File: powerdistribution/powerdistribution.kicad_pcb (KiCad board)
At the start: 4 copper layers, 110 x 75 mm, 128 parts, among them IC1 NCP718ASNADJT1G, J1 282837-2, J2 282837-2, J3 ESQ-113-12-G-D, J6 Conn_01x02, M1 Motor_Servo, M2 Motor_Servo, Q1 IRLML0030, Q2 IRLML0030, Q3 IRLML0030, Q5 IRLML0030, U1 BQ7790512PW, U10 TPS1HC30BQPWPRQ1, U3 AP64501QSP-13, U4 AP64501QSP-13, U5 TPS1HC30BQPWPRQ1, U6 TPS1HC30BQPWPRQ1, U9 MIC29302AWD-TR

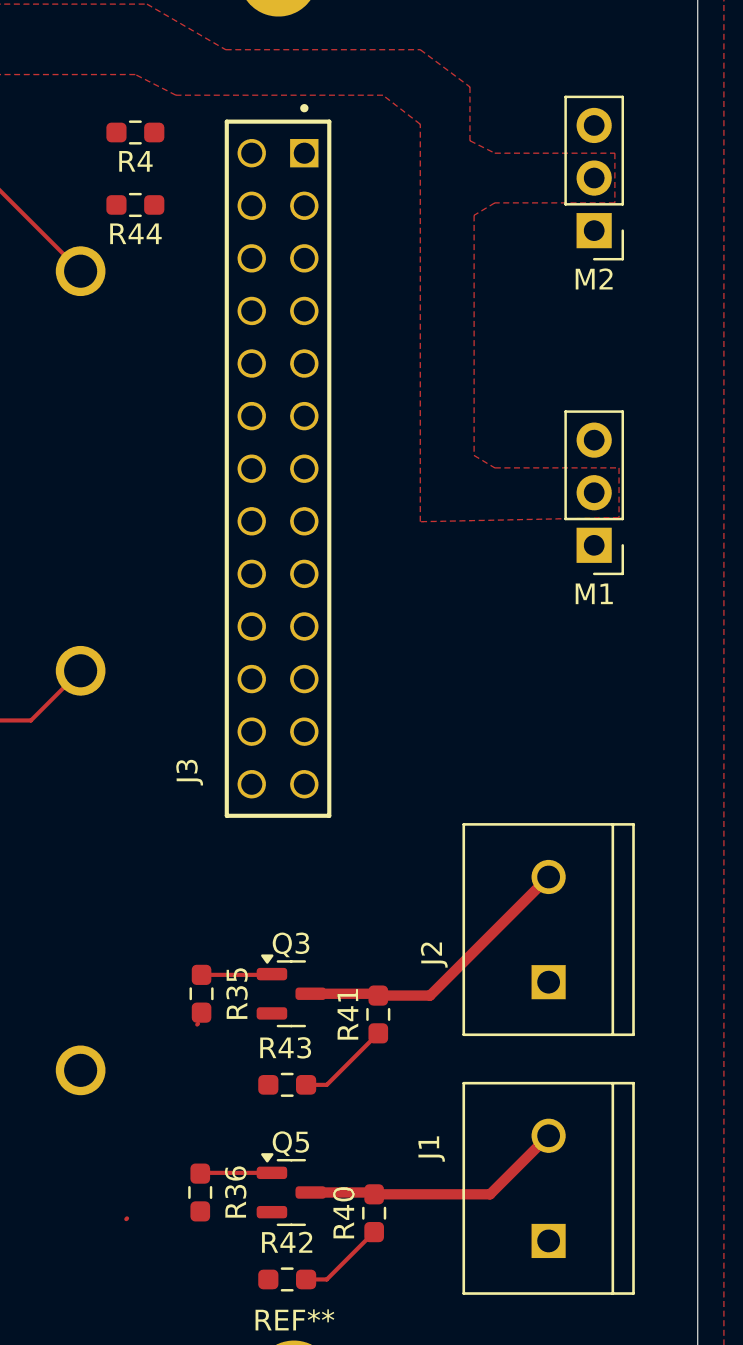
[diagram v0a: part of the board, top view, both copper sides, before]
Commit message: clean up, aligning connectors and board coordinates between fc and power board
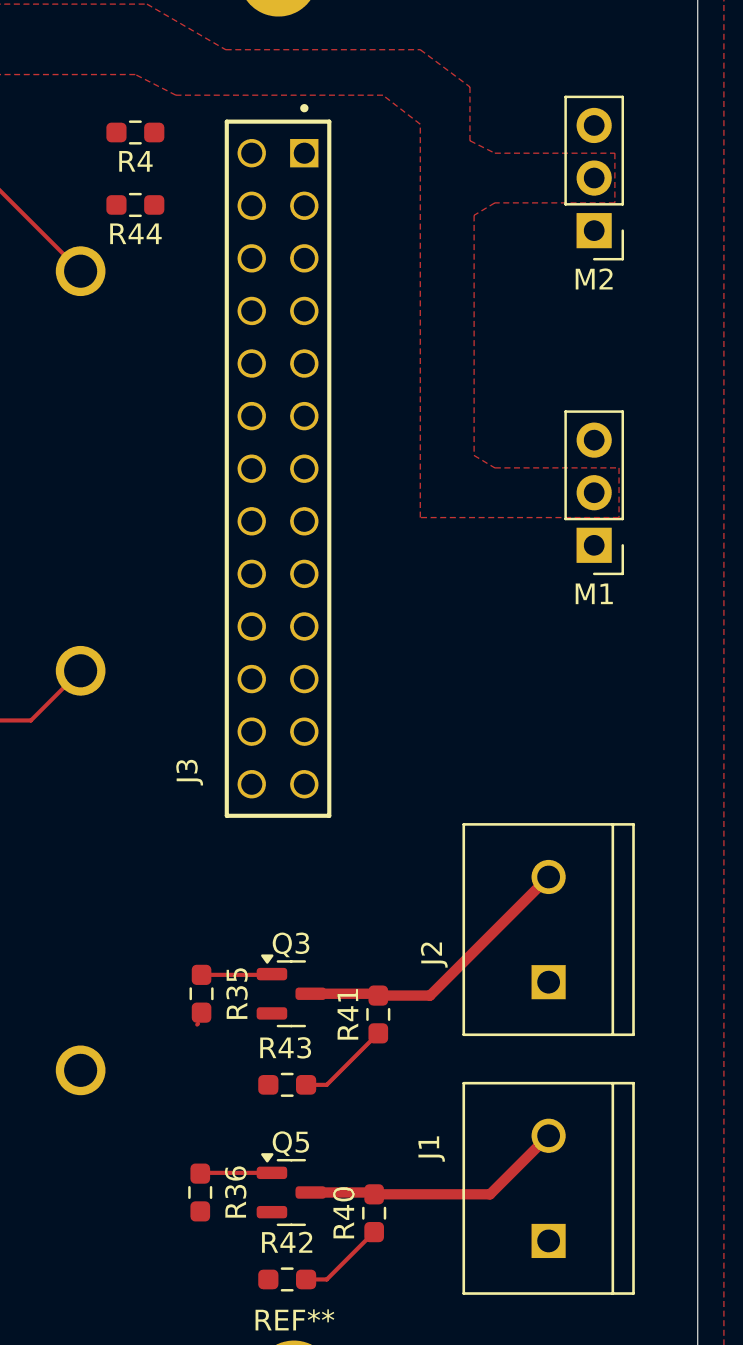
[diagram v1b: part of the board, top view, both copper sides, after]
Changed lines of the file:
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@@
-	)
-	(segment
-		(start 117.4375 126.45)
-		(end 117.4 126.4875)
-		(width 0.2)
-		(layer "F.Cu")
-		(net 21)
 	)
 	(segment
@@
 				(xy 71 69.8) (xy 74 69.8) (xy 75.8 67.8) (xy 118.4 67.8) (xy 122.2 70) (xy 131.6 70) (xy 134 71.8)
 				(xy 134 74.4) (xy 135.2 75) (xy 141 75) (xy 141 77.4) (xy 135.2 77.4) (xy 134.2 78) (xy 134.2 89.6)
-				(xy 135.2 90.2) (xy 141.2 90.2) (xy 141.2 92.6) (xy 131.6 92.8) (xy 131.6 73.6) (xy 129.8 72.2)
+				(xy 135.2 90.2) (xy 141.2 90.2) (xy 141.2 92.6) (xy 131.6 92.6) (xy 131.6 73.6) (xy 129.8 72.2)
 				(xy 119.8 72.2) (xy 117.8375 71.2) (xy 71 71.2)
 			)

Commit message: pd placement finish
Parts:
- removed R4, R44: 0, Resistor_SMD:R_0603_1608Metric_Pad0.98x0.95mm_HandSolder
- added J4: XT60-M, HPRfootprints:AMASS_XT60-M, F.Cu at (139.2, 103.6)
- added TP9: TestPoint, TestPoint:TestPoint_Pad_D2.0mm, F.Cu at (102.0, 104.0)
- added U11: S2P-VH, HPRfootprints:S2P-VH_JST, F.Cu at (132.2, 91.1)
- moved J6 77.8 mm to (136.2, 66.0)
- moved M1 15.6 mm to (135.5, 79.0), turned to 90 degrees
- moved M2 6.59 mm to (135.4, 74.0), turned to 90 degrees
- moved J2 6.29 mm to (138.5, 118.8)
- moved J1 5.25 mm to (137.8, 130.2)
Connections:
- J3 pad 01: unconnected-(J3-Pad01) -> /teensy_3.3v
- J3 pad 02: unconnected-(J3-Pad02) -> /6v_fault
- J3 pad 03: unconnected-(J3-Pad03) -> /servo2_pwm
- J3 pad 04: unconnected-(J3-Pad04) -> /6v_cursns
- J3 pad 05: unconnected-(J3-Pad05) -> /servo1_pwm
- J3 pad 06: unconnected-(J3-Pad06) -> /12v_fault
- J3 pad 08: unconnected-(J3-Pad08) -> /12v_cursns
- J3 pad 10: unconnected-(J3-Pad10) -> /5v_fault
- J3 pad 11: unconnected-(J3-Pad11) -> /PYRO1
- J3 pad 12: unconnected-(J3-Pad12) -> /5v_cursns
- J3 pad 13: unconnected-(J3-Pad13) -> /PYRO1CONN
- J3 pad 14: unconnected-(J3-Pad14) -> /SENSE_mosi
- J3 pad 15: unconnected-(J3-Pad15) -> /PYRO2
- J3 pad 16: unconnected-(J3-Pad16) -> /SENSE_miso
- J3 pad 17: unconnected-(J3-Pad17) -> /PYRO2CONN
- J3 pad 18: unconnected-(J3-Pad18) -> /SENSE_sck
- J3 pad 19: unconnected-(J3-Pad19) -> /5V
- J3 pad 20: unconnected-(J3-Pad20) -> GND
- J3 pad 21: unconnected-(J3-Pad21) -> /5V
- J3 pad 22: unconnected-(J3-Pad22) -> GND
- J3 pad 23: unconnected-(J3-Pad23) -> /5V
- J3 pad 24: unconnected-(J3-Pad24) -> GND
- J3 pad 26: unconnected-(J3-Pad26) -> GND
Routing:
- net /LDO_5V: track 7.42 -> 92.9 mm, vias 1 -> 7
- net /5v_cursns: track 2.98 -> 85.2 mm, vias 0 -> 1
- net /5v_fault: track 0.00 -> 80.7 mm, vias 0 -> 1
- net /12v_cursns: track 2.48 -> 79.1 mm, vias 0 -> 1
- net /12v_fault: track 0.00 -> 74.6 mm, vias 0 -> 1
- net /6v_cursns: track 2.73 -> 73.4 mm, vias 0 -> 1
- net /6v_fault: track 0.00 -> 69.2 mm, vias 0 -> 1
- net /PYRO1CONN: track 4.24 -> 46.6 mm, vias 0 -> 1
- net /PYRO1: track 3.42 -> 41.2 mm, vias 0 -> 1
- net /PYRO2CONN: track 4.52 -> 28.2 mm, vias 0 -> 1
- net /PYRO2: track 3.36 -> 26.1 mm, vias 0 -> 1
- net /servo2_pwm: track 0.00 -> 10.9 mm
- net /servo1_pwm: track 0.00 -> 9.95 mm
- net /Pack+: track 23.9 -> 16.3 mm
- net /5V_DIAGEN: track 7.52 -> 12.7 mm
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- added copper zone on F.Cu, net /5V
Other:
- board text removed: "${REFERENCE}"

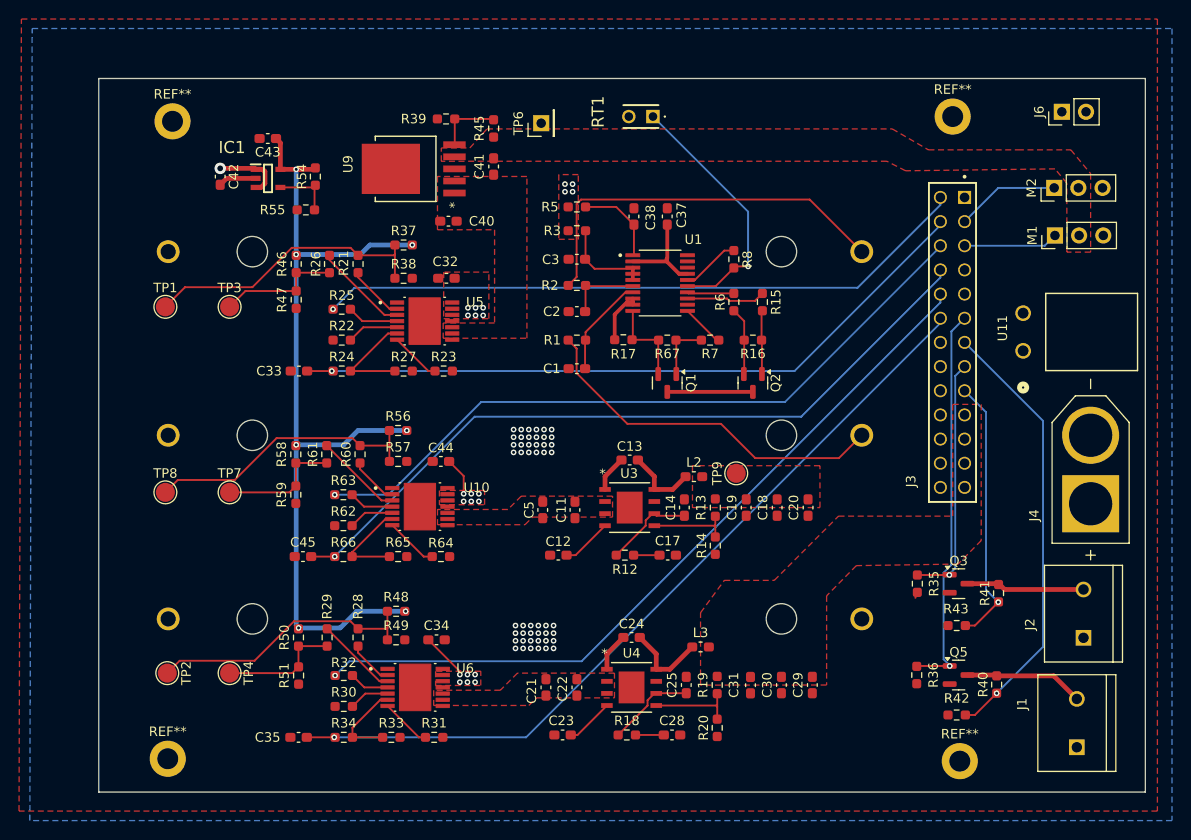
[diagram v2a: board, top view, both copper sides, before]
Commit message: hole+connector alignment finish, fc signal routing finish, fc drc warnings related to footprints/silkscreen
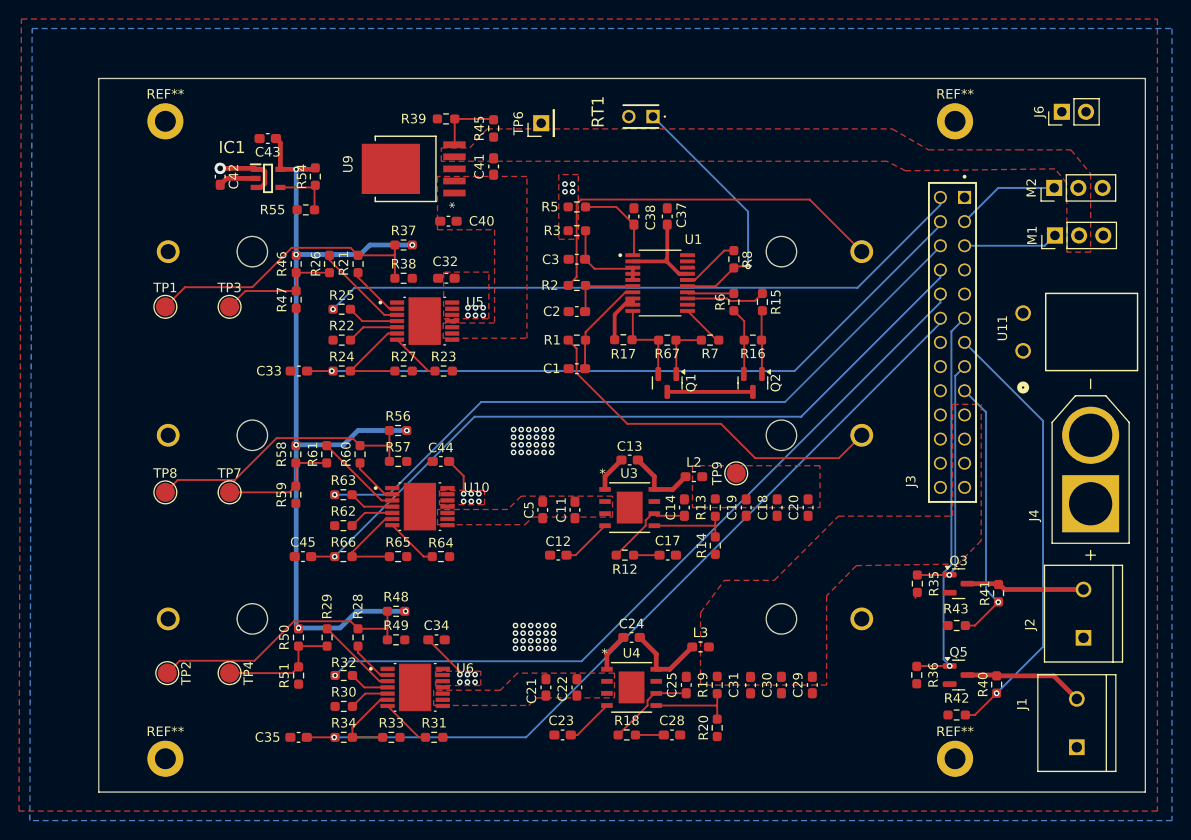
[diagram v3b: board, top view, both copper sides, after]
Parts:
- moved REF** 0.75 mm to (42.0, 67.0)
- moved REF** 0.56 mm to (125.0, 134.0)
- moved REF** 0.56 mm to (125.0, 67.0)
- moved REF** 0.25 mm to (42.0, 134.0)
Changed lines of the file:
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@@
 	(footprint "MountingHole:MountingHole_2.2mm_M2_DIN965_Pad"
 		(layer "F.Cu")
-		(at 125.5 134.25)
+		(at 125 134)
 		(descr "Mounting Hole 2.2mm, M2, generated by kicad-footprint-generator mountinghole.py")
 		(tags "mountinghole M2 DIN965")
@@
 	(footprint "MountingHole:MountingHole_2.2mm_M2_DIN965_Pad"
 		(layer "F.Cu")
-		(at 124.75 66.5)
+		(at 125 67)
 		(descr "Mounting Hole 2.2mm, M2, generated by kicad-footprint-generator mountinghole.py")
 		(tags "mountinghole M2 DIN965")
@@
 	(footprint "MountingHole:MountingHole_2.2mm_M2_DIN965_Pad"
 		(layer "F.Cu")
-		(at 42.25 134)
+		(at 42 134)
 		(descr "Mounting Hole 2.2mm, M2, generated by kicad-footprint-generator mountinghole.py")
 		(tags "mountinghole M2 DIN965")
@@
 	(footprint "MountingHole:MountingHole_2.2mm_M2_DIN965_Pad"
 		(layer "F.Cu")
-		(at 42.75 67)
+		(at 42 67)
 		(descr "Mounting Hole 2.2mm, M2, generated by kicad-footprint-generator mountinghole.py")
 		(tags "mountinghole M2 DIN965")

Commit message: killed BMS, updated pyro fets with lower resistance, updated inductor, replace + reroute, fixed some DRC in flight computer (dont know why remaining are being caused, hopefully jlc doesnt care), next todo is to kill myself
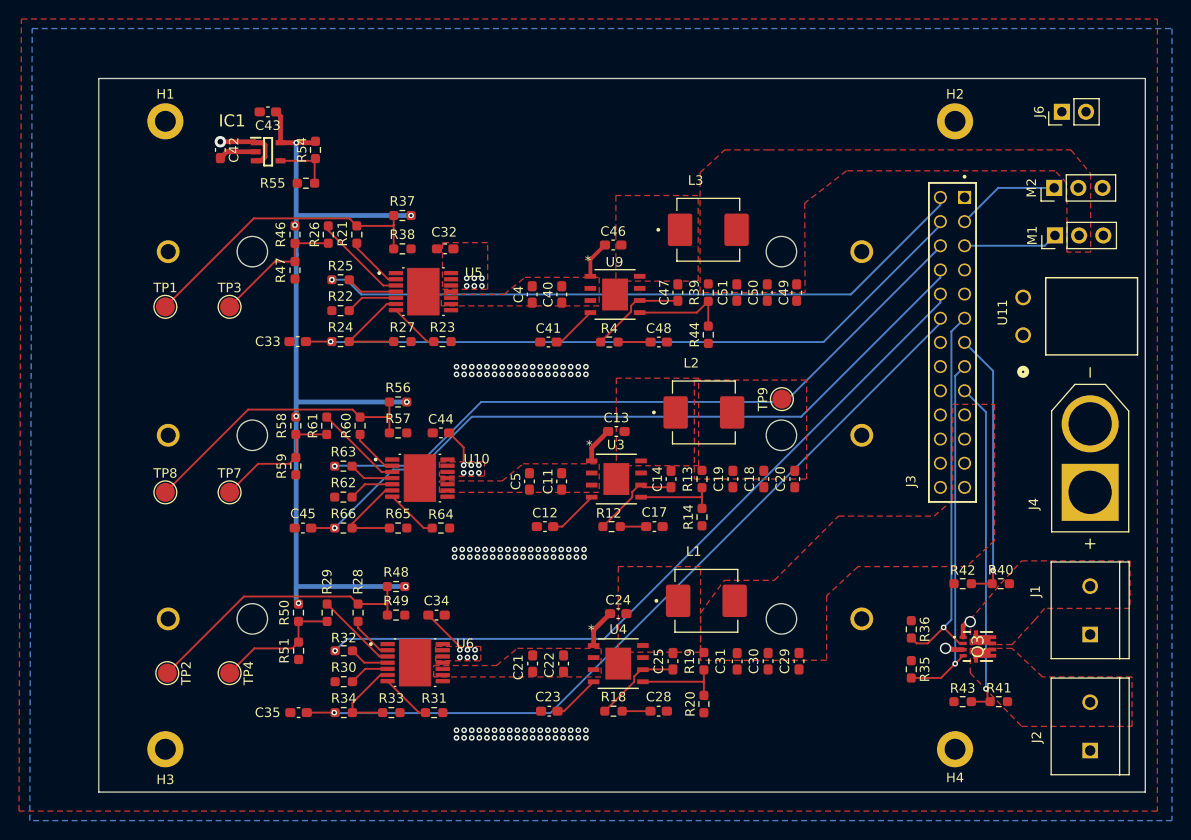
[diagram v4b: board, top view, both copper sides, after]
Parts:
- removed C1, C2, C3: 0.1μF, Capacitor_SMD:C_0603_1608Metric_Pad1.08x0.95mm_HandSolder
- removed C37, C38: C_Small, Capacitor_SMD:C_0603_1608Metric_Pad1.08x0.95mm_HandSolder
- removed Q1, Q2, Q5: IRLML0030, Package_TO_SOT_SMD:SOT-23
- removed R1, R2, R3, R5: 1K, Resistor_SMD:R_0603_1608Metric_Pad0.98x0.95mm_HandSolder
- removed R15, R16, R17, R6, R67, R7, R8: R_Small, Resistor_SMD:R_0603_1608Metric_Pad0.98x0.95mm_HandSolder
- removed R45: 4.7k, Resistor_SMD:R_0603_1608Metric_Pad0.98x0.95mm_HandSolder
- removed REF** (x4): MountingHole_2.2mm_M2_DIN965_Pad, MountingHole:MountingHole_2.2mm_M2_DIN965_Pad
- removed RT1: 103AT-2, HPRfootprints:103AT2
- removed TP6: TestPoint, Connector_PinHeader_2.54mm:PinHeader_1x01_P2.54mm_Vertical
- removed U1: BQ7790512PW, HPRfootprints:SOP65P640X120-20N
- added C4: 10uf, Capacitor_SMD:C_0603_1608Metric_Pad1.08x0.95mm_HandSolder, F.Cu at (80.6, 85.2)
- added C46: 100nF, Capacitor_SMD:C_0603_1608Metric_Pad1.08x0.95mm_HandSolder, F.Cu at (89.1, 80.0)
- added C47: 33pf, Capacitor_SMD:C_0603_1608Metric_Pad1.08x0.95mm_HandSolder, F.Cu at (95.9, 85.0)
- added C48: 2.7nf, Capacitor_SMD:C_0603_1608Metric_Pad1.08x0.95mm_HandSolder, F.Cu at (93.9, 90.2)
- added C49: 22 uf, Capacitor_SMD:C_0603_1608Metric_Pad1.08x0.95mm_HandSolder, F.Cu at (108.4, 85.0)
- added C50: 22 uf, Capacitor_SMD:C_0603_1608Metric_Pad1.08x0.95mm_HandSolder, F.Cu at (105.3, 85.0)
- added C51: 22uf, Capacitor_SMD:C_0603_1608Metric_Pad1.08x0.95mm_HandSolder, F.Cu at (102.1, 85.0)
- added H1: MountingHole_Pad, MountingHole:MountingHole_2.2mm_M2_DIN965_Pad, F.Cu at (42.0, 67.0)
- added H2: MountingHole_Pad, MountingHole:MountingHole_2.2mm_M2_DIN965_Pad, F.Cu at (125.0, 67.0)
- added H3: MountingHole_Pad, MountingHole:MountingHole_2.2mm_M2_DIN965_Pad, F.Cu at (42.0, 133.0)
- added H4: MountingHole_Pad, MountingHole:MountingHole_2.2mm_M2_DIN965_Pad, F.Cu at (125.0, 133.0)
- added L1: CSAB0730-4R7M, HPRlibrary:CSAB0730-4R7M, F.Cu at (98.9, 117.4)
- added R4: 10.5k, Resistor_SMD:R_0603_1608Metric_Pad0.98x0.95mm_HandSolder, F.Cu at (88.7, 90.2)
- added R44: 10k, Resistor_SMD:R_0603_1608Metric_Pad0.98x0.95mm_HandSolder, F.Cu at (99.1, 89.4)
- C40: value 10uF -> 10uf
- C41: value 22uF -> 10nf
- L2: value 6.8 uh -> CSAB0730-3R3M; footprint Inductor_SMD:L_0603_1608Metric_Pad1.05x0.95mm_HandSolder -> HPRlibrary:CSAB0730-3R3M
- L3: value 6.8 uh -> CSAB0730-4R7M; footprint Inductor_SMD:L_0603_1608Metric_Pad1.05x0.95mm_HandSolder -> HPRlibrary:CSAB0730-4R7M
- Q3: value IRLML0030 -> SI7232DN-T1-GE3; footprint Package_TO_SOT_SMD:SOT-23 -> HPRlibrary:SI7232DNT1GE3
- R23, R31, R64: value ~ -> 10k
- R39: value 1.2k -> 65k
- U9: value MIC29302AWD-TR -> AP64501QSP-13; footprint HPRfootprints:TO-252-5_MCH -> HPRfootprints:SO-8EP_DIO-L
- moved L3 43.9 mm to (99.1, 78.4), turned to 0 degrees
- moved R39 33.1 mm to (99.1, 85.0), turned to -90 degrees
- moved U9 25.7 mm to (89.3, 85.2), turned to 0 degrees
- moved C41 19.3 mm to (82.3, 90.2), turned to 0 degrees
- moved C40 14.2 mm to (83.7, 85.2), turned to 90 degrees
- moved R42 13.8 mm to (125.8, 115.6)
- moved J1 11.9 mm to (139.2, 118.4)
- moved J2 11.9 mm to (139.2, 130.6)
- moved R41 11.4 mm to (129.6, 128.0), turned to 0 degrees
- moved R40 10.6 mm to (129.8, 115.6), turned to 0 degrees
- moved TP9 9.16 mm to (106.8, 96.2)
- moved R35 9.02 mm to (120.4, 124.6), turned to -90 degrees
- moved R43 8.02 mm to (125.8, 128.0)
- moved Q3 6.90 mm to (127.4, 122.2), turned to -90 degrees
- moved L2 6.83 mm to (98.6, 97.6), turned to 0 degrees
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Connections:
- net /12V_DIAGEN renamed /3.3V_DIAGEN
- net /12V_EN renamed /3.3V_EN
- net /12v_cursns renamed /3.3v_cursns
- net /12v_fault renamed /3.3v_fault
- net /XV_SWout renamed /3.3V_SWout
- C13 pad 2: Net-(U3-SW) -> /3.3V_LIN
- C18 pad 1: /12V -> /3.3V
- C19 pad 1: /12V -> /3.3V
- C20 pad 1: /12V -> /3.3V
- C24 pad 2: Net-(U4-SW) -> /5V_LIN
- C40 pad 1: /6V_SWout -> GND
- C40 pad 2: GND -> /6V_SWout
- C41 pad 1: /6V -> GND
- C41 pad 2: GND -> Net-(U9-SS)
- J1 pad 2: Net-(Q5-D) -> /PYROOUT1
- J2 pad 2: Net-(Q3-D) -> /PYROOUT2
- L2 pad 1: /12V -> /3.3V_LIN
- L2 pad 2: Net-(U3-SW) -> /3.3V
- L3 pad 1: /5V -> /6V_LIN
- L3 pad 2: Net-(U4-SW) -> /6V
- Q3 pad 1: /PYRO2 -> GND
- Q3 pad 2: GND -> /PYRO1
- Q3 pad 3: Net-(Q3-D) -> GND
- R13 pad 1: /12V -> /3.3V
- R39 pad 1: Net-(U9-ADJ) -> /6V
- R39 pad 2: GND -> Net-(U9-FB)
- R40 pad 2: Net-(Q5-D) -> /PYROOUT1
- R41 pad 2: Net-(Q3-D) -> /PYROOUT2
- TP9 pad 1: /12V -> /3.3V
- U3 pad 8: Net-(U3-SW) -> /3.3V_LIN
- U4 pad 8: Net-(U4-SW) -> /5V_LIN
- U9 pad 1: /6V_SWout -> Net-(U9-BST)
- U9 pad 3: GND -> /6V_SWout
- U9 pad 4: /6V -> Net-(U9-SS)
- U9 pad 5: Net-(U9-ADJ) -> Net-(U9-FB)
- U9 pad 6: GND -> Net-(U9-COMP)
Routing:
- net /B2: track 41.4 -> 0.00 mm
- net /B1: track 38.5 -> 0.00 mm
- net Net-(U1-TS): track 27.1 -> 0.00 mm, vias 1 -> 0
- net /PYRO1CONN: track 46.6 -> 28.8 mm
- net Net-(Q5-D): track 12.5 -> 0.00 mm
- net Net-(Q3-D): track 12.4 -> 0.00 mm
- net /PYRO2: track 26.1 -> 38.1 mm
- net Net-(U1-VC1): track 10.6 -> 0.00 mm
- net Net-(U9-FB): track 0.00 -> 10.3 mm
- net Net-(U9-COMP): track 0.00 -> 10.3 mm
- net Net-(U1-AVDD): track 10.2 -> 0.00 mm
- net Net-(U1-VC3): track 9.75 -> 0.00 mm
- net Net-(Q1-S): track 9.45 -> 0.00 mm
- net Net-(U1-VDD): track 9.12 -> 0.00 mm
- net Net-(Q1-D): track 9.00 -> 0.00 mm
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- added copper zone on F.Cu, net /3.3V
- added copper zone on F.Cu, net /3.3V_LIN
- added copper zone on F.Cu, net /5V_LIN
- added copper zone on F.Cu, net /6V_LIN
- added copper zone on F.Cu, net /PYROOUT1
- added copper zone on F.Cu, net /PYROOUT2
- removed copper zone on F.Cu, net /12V
